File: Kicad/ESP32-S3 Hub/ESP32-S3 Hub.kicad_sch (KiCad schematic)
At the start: 25 parts, among them U1 ESP32-S3, Y1 40mhz, 10ppm, 12pF

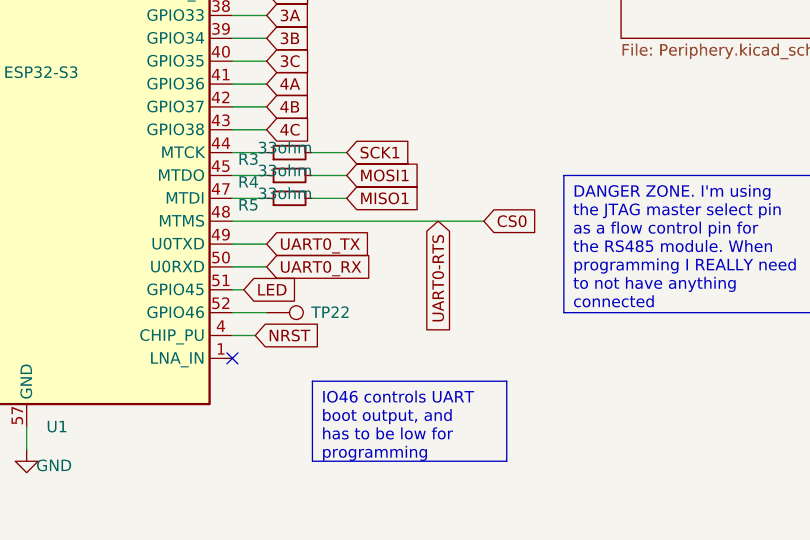
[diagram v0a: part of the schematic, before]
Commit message: Fixed ERC errors, stopped tracking a few .obsidian files
The only errors that popped up were the dual labeling of CS0 and Uart RTS, a power flag spot, and a modified footprint error.
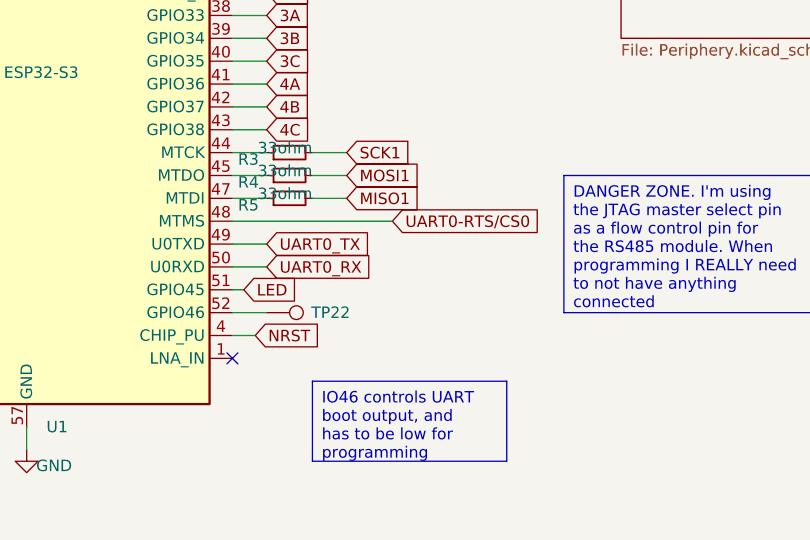
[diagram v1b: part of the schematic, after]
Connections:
- net CS0 renamed UART0-RTS/CS0
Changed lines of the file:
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@@
 	(wire
 		(pts
-			(xy 167.64 107.95) (xy 195.58 107.95)
+			(xy 167.64 107.95) (xy 185.42 107.95)
 		)
 		(stroke
@@
 		)
 	)
-	(global_label "UART0-RTS"
-		(shape input)
-		(at 190.5 107.95 270)
+	(global_label "UART0-RTS{slash}CS0"
+		(shape input)
+		(at 185.42 107.95 0)
+		(fields_autoplaced yes)
+		(effects
+			(font
+				(size 1.27 1.27)
+			)
+			(justify left)
+		)
+		(property "Intersheetrefs" "${INTERSHEET_REFS}"
+			(at 204.3104 107.95 0)
+			(effects
+				(font
+					(size 1.27 1.27)
+				)
+				(justify left)
+				(hide yes)
+			)
+		)
+	)
+	(global_label "4CSA-B"
+		(shape input)
+		(at 118.11 85.09 180)
 		(fields_autoplaced yes)
 		(effects
@@
 		)
 		(property "Intersheetrefs" "${INTERSHEET_REFS}"
-			(at 190.5 121.8209 90)
+			(at 107.5048 85.09 0)
 			(effects
 				(font
@@
 				(hide yes)
 			)
-		)
-	)
-	(global_label "4CSA-B"
-		(shape input)
-		(at 118.11 85.09 180)
-		(fields_autoplaced yes)
-		(effects
-			(font
-				(size 1.27 1.27)
-			)
-			(justify right)
-		)
-		(property "Intersheetrefs" "${INTERSHEET_REFS}"
-			(at 107.5048 85.09 0)
-			(effects
-				(font
-					(size 1.27 1.27)
-				)
-				(justify right)
-				(hide yes)
-			)
-		)
-	)
-	(global_label "CS0"
-		(shape input)
-		(at 195.58 107.95 0)
-		(fields_autoplaced yes)
-		(effects
-			(font
-				(size 1.27 1.27)
-			)
-			(justify left)
-		)
-		(property "Intersheetrefs" "${INTERSHEET_REFS}"
-			(at 202.2542 107.95 0)
-			(effects
-				(font
-					(size 1.27 1.27)
-				)
-				(justify left)
-				(hide yes)
-			)

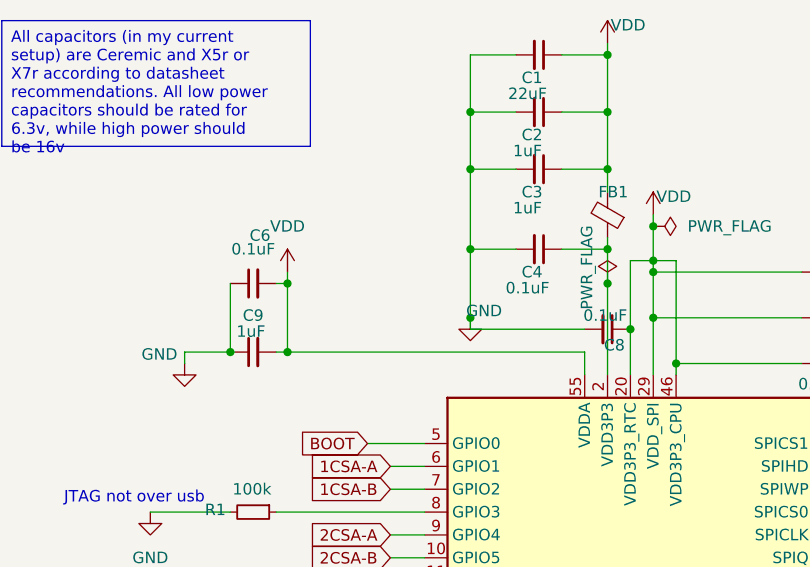
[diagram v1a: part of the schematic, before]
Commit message: Started Layout
I added the footprints on the PCB file. My goal is to fit everything within a 15x30mm package. We will see!
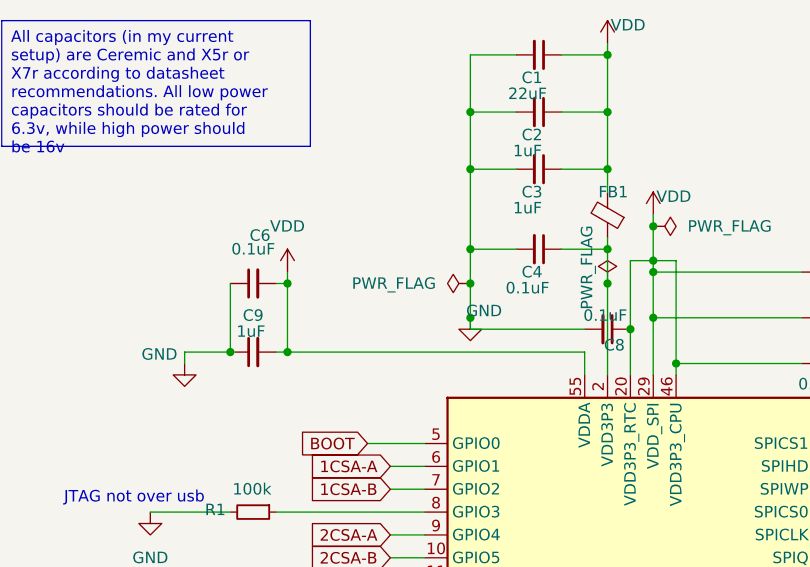
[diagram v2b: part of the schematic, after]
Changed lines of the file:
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@@
+	)
+	(junction
+		(at 127 44.45)
+		(diameter 0)
+		(color 0 0 0 0)
 	)
 	(junction
@@
 	(wire
 		(pts
+			(xy 127 44.45) (xy 127 48.26)
+		)
+		(stroke
+			(width 0)
+			(type default)
+		)
+	)
+	(wire
+		(pts
 			(xy 127 49.53) (xy 139.7 49.53)
 		)
@@
 	(wire
 		(pts
-			(xy 127 40.64) (xy 127 48.26)
+			(xy 127 40.64) (xy 127 44.45)
 		)
 		(stroke
@@
 					(unit 1)
 				)
+			)
+		)
+	)
+	(symbol
+		(lib_id "power:PWR_FLAG")
+		(at 127 44.45 90)
+		(unit 1)
+		(exclude_from_sim no)
+		(in_bom yes)
+		(on_board yes)
+		(dnp no)
+		(fields_autoplaced yes)
+		(property "Reference" "#FLG03"
+			(at 125.095 44.45 0)
+			(effects
+				(font
+					(size 1.27 1.27)
+				)
+				(hide yes)
+			)
+		)
+		(property "Value" "PWR_FLAG"
+			(at 123.19 44.4499 90)
+			(effects
+				(font
+					(size 1.27 1.27)
+				)
+				(justify left)
+			)
+		)
+		(property "Footprint" ""
+			(at 127 44.45 0)
+			(effects
+				(font
+					(size 1.27 1.27)
+				)
+				(hide yes)
+			)
+		)
+		(property "Datasheet" "~"
+			(at 127 44.45 0)
+			(effects
+				(font
+					(size 1.27 1.27)
+				)
+				(hide yes)
+			)
+		)
+		(property "Description" "Special symbol for telling ERC where power comes from"
+			(at 127 44.45 0)
+			(effects
+				(font
+					(size 1.27 1.27)
+				)
+				(hide yes)
+			)
+		)
+		(pin "1"
+		)
+		(instances
+			(project "ESP32-S3 Hub"
+				(path "/a8c80fba-3bca-4358-b5bb-9ebf9383c658"
+					(reference "#FLG03")
+					(unit 1)
+				)

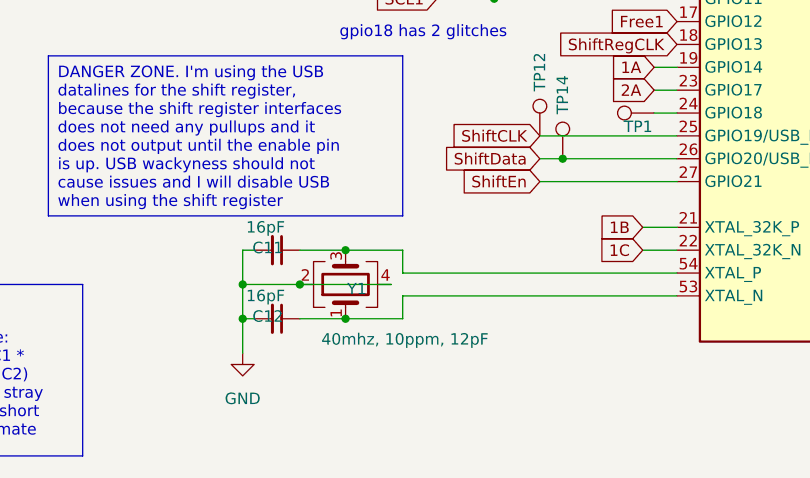
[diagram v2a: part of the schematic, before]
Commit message: Switching out footprints for smaller variants, dropping rs485 resistors
Space is tight, so I had to downsize the crystal and the reset switches. I also don't have space for the rs485 termination resistors configurable per device, so I have excluded this from the board.
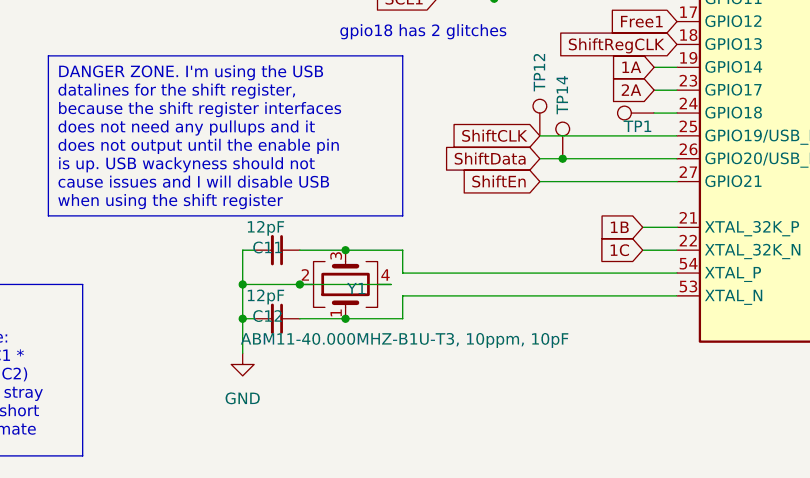
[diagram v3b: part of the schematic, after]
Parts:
- C1, C10, C2, C3, C4, C5, C6, C7, C8, C9: footprint Capacitor_SMD:C_0603_1608Metric -> Capacitor_SMD:C_0402_1005Metric
- C11, C12: value 16pF -> 12pF; footprint Capacitor_SMD:C_0603_1608Metric_Pad1.08x0.95mm_HandSolder -> Capacitor_SMD:C_0402_1005Metric
- R1, R3, R4, R5, R8, R9: footprint Resistor_SMD:R_0603_1608Metric -> Resistor_SMD:R_0402_1005Metric
- Y1: value 40mhz, 10ppm, 12pF -> ABM11-40.000MHZ-B1U-T3, 10ppm, 10pF; footprint Crystal:Crystal_SMD_3225-4Pin_3.2x2.5mm -> Crystal:Crystal_SMD_2016-4Pin_2.0x1.6mm
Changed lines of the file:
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@@
 			)
 		)
-		(property "Value" "40mhz, 10ppm, 12pF"
+		(property "Value" "ABM11-40.000MHZ-B1U-T3, 10ppm, 10pF"
 			(at 91.694 128.016 90)
 			(effects
@@
 			)
 		)
-		(property "Footprint" "Crystal:Crystal_SMD_3225-4Pin_3.2x2.5mm"
+		(property "Footprint" "Crystal:Crystal_SMD_2016-4Pin_2.0x1.6mm"
 			(at 85.09 121.92 0)
 			(effects
@@
 			)
 		)
-		(property "Footprint" "Capacitor_SMD:C_0603_1608Metric"
+		(property "Footprint" "Capacitor_SMD:C_0402_1005Metric"
 			(at 102.87 52.07 0)
 			(effects
@@
 			)
 		)
-		(property "Footprint" "Capacitor_SMD:C_0603_1608Metric"
+		(property "Footprint" "Capacitor_SMD:C_0402_1005Metric"
 			(at 102.87 44.45 0)
 			(effects
@@
 			)
 		)
-		(property "Footprint" "Capacitor_SMD:C_0603_1608Metric"
+		(property "Footprint" "Capacitor_SMD:C_0402_1005Metric"
 			(at 142.24 49.53 0)
 			(effects
@@
 			)
 		)
-		(property "Footprint" "Resistor_SMD:R_0603_1608Metric"
+		(property "Footprint" "Resistor_SMD:R_0402_1005Metric"
 			(at 99.06 85.09 0)
 			(effects
@@
 			)
 		)
-		(property "Footprint" "Capacitor_SMD:C_0603_1608Metric"
+		(property "Footprint" "Capacitor_SMD:C_0402_1005Metric"
 			(at 166.37 43.18 0)
 			(effects
@@
 			)
 		)
-		(property "Footprint" "Capacitor_SMD:C_0603_1608Metric"
+		(property "Footprint" "Capacitor_SMD:C_0402_1005Metric"
 			(at 134.62 31.75 0)
 			(effects
@@
 			)
 		)
-		(property "Value" "16pF"
+		(property "Value" "12pF"
 			(at 76.2 123.19 90)
 			(effects
@@
 			)
 		)
-		(property "Footprint" "Capacitor_SMD:C_0603_1608Metric_Pad1.08x0.95mm_HandSolder"
+		(property "Footprint" "Capacitor_SMD:C_0402_1005Metric"
 			(at 77.47 125.73 0)
 			(effects
@@
 			)
 		)
-		(property "Footprint" "Capacitor_SMD:C_0603_1608Metric"
+		(property "Footprint" "Capacitor_SMD:C_0402_1005Metric"
 			(at 134.62 40.64 0)
 			(effects
@@
 			)
 		)
-		(property "Footprint" "Resistor_SMD:R_0603_1608Metric"
+		(property "Footprint" "Resistor_SMD:R_0402_1005Metric"
 			(at 173.99 100.33 0)
 			(effects
@@
 			)
 		)
-		(property "Footprint" "Resistor_SMD:R_0603_1608Metric"
+		(property "Footprint" "Resistor_SMD:R_0402_1005Metric"
 			(at 101.6 87.63 0)
 			(effects
@@
 			)
 		)
-		(property "Footprint" "Resistor_SMD:R_0603_1608Metric"
+		(property "Footprint" "Resistor_SMD:R_0402_1005Metric"
 			(at 173.99 105.41 0)
 			(effects
@@
 			)
 		)
-		(property "Footprint" "Capacitor_SMD:C_0603_1608Metric"
+		(property "Footprint" "Capacitor_SMD:C_0402_1005Metric"
 			(at 166.37 53.34 0)
 			(effects
@@
 			)
 		)
-		(property "Footprint" "Capacitor_SMD:C_0603_1608Metric"
+		(property "Footprint" "Capacitor_SMD:C_0402_1005Metric"
 			(at 134.62 25.4 0)
 			(effects
@@
 			)
 		)
-		(property "Footprint" "Resistor_SMD:R_0603_1608Metric"
+		(property "Footprint" "Resistor_SMD:R_0402_1005Metric"
 			(at 173.99 102.87 0)
 			(effects
@@
 			)
 		)
-		(property "Footprint" "Capacitor_SMD:C_0603_1608Metric"
+		(property "Footprint" "Capacitor_SMD:C_0402_1005Metric"
 			(at 166.37 48.26 0)
 			(effects
@@
 			)
 		)
-		(property "Footprint" "Resistor_SMD:R_0603_1608Metric"
+		(property "Footprint" "Resistor_SMD:R_0402_1005Metric"
 			(at 102.87 69.85 0)
 			(effects
@@
 			)
 		)
-		(property "Footprint" "Capacitor_SMD:C_0603_1608Metric"
+		(property "Footprint" "Capacitor_SMD:C_0402_1005Metric"
 			(at 134.62 19.05 0)
 			(effects
@@
 			)
 		)
-		(property "Value" "16pF"
+		(property "Value" "12pF"
 			(at 76.2 115.57 90)
 			(effects
@@
 			)
 		)
-		(property "Footprint" "Capacitor_SMD:C_0603_1608Metric_Pad1.08x0.95mm_HandSolder"
+		(property "Footprint" "Capacitor_SMD:C_0402_1005Metric"
 			(at 77.47 118.11 0)
 			(effects

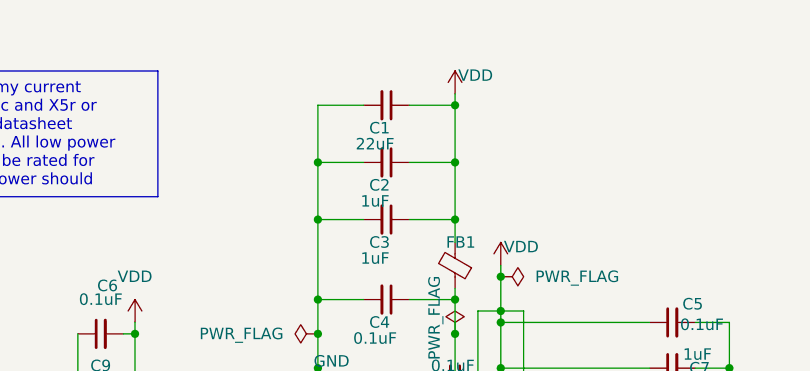
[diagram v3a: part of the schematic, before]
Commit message: Finished basic layout
Everything is crammed in there, I do have some extras bit of space up top for an extra component or two. I probably should take advantage of that space somehow. For routing this thing, I really think i need a 6 or 8 layer board with blind vias.
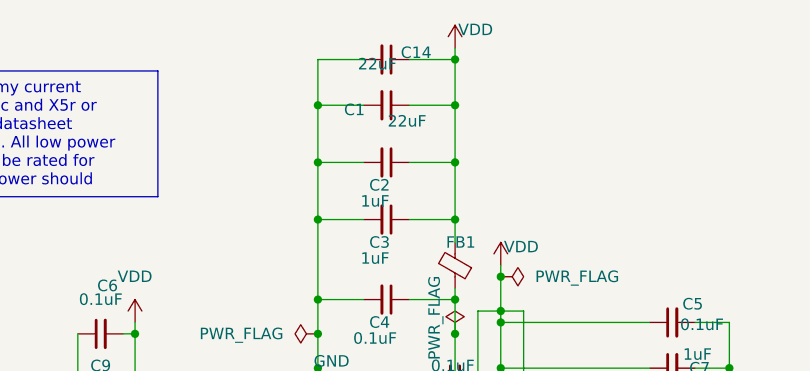
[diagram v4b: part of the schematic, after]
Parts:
- added C14: 22uF, Capacitor_SMD:C_0402_1005Metric, symbol Device:C_Small
- FB1: value 120ohm imp @100mhz -> 120ohm imp @100mhz, 1 amp; footprint Inductor_SMD:L_0603_1608Metric -> Inductor_SMD:L_0402_1005Metric
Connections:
- net GND: now also C14.2
- net VDD: now also C14.1
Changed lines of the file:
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@@
 	)
 	(junction
+		(at 142.24 13.97)
+		(diameter 0)
+		(color 0 0 0 0)
+	)
+	(junction
 		(at 73.66 125.73)
 		(diameter 0)
@@
 	)
 	(junction
+		(at 127 19.05)
+		(diameter 0)
+		(color 0 0 0 0)
+	)
+	(junction
 		(at 109.22 107.95)
 		(diameter 0)
@@
 	(wire
 		(pts
+			(xy 132.08 13.97) (xy 127 13.97)
+		)
+		(stroke
+			(width 0)
+			(type default)
+		)
+	)
+	(wire
+		(pts
 			(xy 142.24 44.45) (xy 142.24 54.61)
 		)
@@
 	(wire
 		(pts
-			(xy 142.24 17.78) (xy 142.24 19.05)
+			(xy 142.24 12.7) (xy 142.24 13.97)
 		)
 		(stroke
@@
 	(wire
 		(pts
+			(xy 142.24 13.97) (xy 142.24 19.05)
+		)
+		(stroke
+			(width 0)
+			(type default)
+		)
+	)
+	(wire
+		(pts
 			(xy 105.41 44.45) (xy 106.68 44.45)
 		)
@@
 	(wire
 		(pts
+			(xy 127 13.97) (xy 127 19.05)
+		)
+		(stroke
+			(width 0)
+			(type default)
+		)
+	)
+	(wire
+		(pts
 			(xy 127 25.4) (xy 127 31.75)
 		)
@@
 	(wire
 		(pts
+			(xy 127 19.05) (xy 127 25.4)
+		)
+		(stroke
+			(width 0)
+			(type default)
+		)
+	)
+	(wire
+		(pts
 			(xy 147.32 36.83) (xy 147.32 38.1)
 		)
@@
 	(wire
 		(pts
+			(xy 137.16 13.97) (xy 142.24 13.97)
+		)
+		(stroke
+			(width 0)
+			(type default)
+		)
+	)
+	(wire
+		(pts
 			(xy 127 40.64) (xy 127 44.45)
 		)
@@
 	(wire
 		(pts
-			(xy 127 19.05) (xy 127 25.4)
-		)
-		(stroke
-			(width 0)
-			(type default)
-		)
-	)
-	(wire
-		(pts
 			(xy 106.68 105.41) (xy 121.92 105.41)
 		)
@@
 			)
 		)
-		(property "Value" "120ohm imp @100mhz"
+		(property "Value" "120ohm imp @100mhz, 1 amp"
 			(at 137.16 38.608 0)
 			(effects
@@
 			)
 		)
-		(property "Footprint" "Inductor_SMD:L_0603_1608Metric"
+		(property "Footprint" "Inductor_SMD:L_0402_1005Metric"
 			(at 144.018 36.83 90)
 			(effects
@@
 	(symbol
 		(lib_id "power:VDD")
-		(at 142.24 17.78 0)
+		(at 142.24 12.7 0)
 		(unit 1)
 		(exclude_from_sim no)
@@
 		(dnp no)
 		(property "Reference" "#PWR01"
-			(at 142.24 21.59 0)
+			(at 142.24 16.51 0)
 			(effects
 				(font
@@
 		)
 		(property "Value" "VDD"
-			(at 144.526 15.748 0)
+			(at 144.526 10.668 0)
 			(effects
 				(font
@@
 		)
 		(property "Footprint" ""
-			(at 142.24 17.78 0)
+			(at 142.24 12.7 0)
 			(effects
 				(font
@@
 		)
 		(property "Datasheet" ""
-			(at 142.24 17.78 0)
+			(at 142.24 12.7 0)
 			(effects
 				(font
@@
 		)
 		(property "Description" "Power symbol creates a global label with name \"VDD\""
-			(at 142.24 17.78 0)
+			(at 142.24 12.7 0)
 			(effects
 				(font
@@
 	)
 	(symbol
+		(lib_id "Device:C_Small")
+		(at 134.62 13.97 270)
+		(unit 1)
+		(exclude_from_sim no)
+		(in_bom yes)
+		(on_board yes)
+		(dnp no)
+		(property "Reference" "C14"
+			(at 137.922 13.208 90)
+			(effects
+				(font
+					(size 1.27 1.27)
+				)
+			)
+		)
+		(property "Value" "22uF"
+			(at 133.604 14.478 90)
+			(effects
+				(font
+					(size 1.27 1.27)
+				)
+			)
+		)
+		(property "Footprint" "Capacitor_SMD:C_0402_1005Metric"
+			(at 134.62 13.97 0)
+			(effects
+				(font
+					(size 1.27 1.27)
+				)
+				(hide yes)
+			)
+		)
+		(property "Datasheet" "~"
+			(at 134.62 13.97 0)
+			(effects
+				(font
+					(size 1.27 1.27)
+				)
+				(hide yes)
+			)
+		)
+		(property "Description" "Unpolarized capacitor, small symbol"
+			(at 134.62 13.97 0)
+			(effects
+				(font
+					(size 1.27 1.27)
+				)
+				(hide yes)
+			)
+		)
+		(pin "2"
+		)
+		(pin "1"
+		)
+		(instances
+			(project "ESP32-S3 Hub"
+				(path "/a8c80fba-3bca-4358-b5bb-9ebf9383c658"
+					(reference "C14")
+					(unit 1)
+				)
+			)
+		)
+	)
+	(symbol
 		(lib_id "Device:R_Small")
 		(at 102.87 69.85 270)
@@
 		(dnp no)
 		(property "Reference" "C1"
-			(at 133.858 21.59 90)
+			(at 131.064 19.558 90)
 			(effects
 				(font
@@
 		)
 		(property "Value" "22uF"
-			(at 133.35 23.368 90)
+			(at 136.906 20.828 90)
 			(effects
 				(font
